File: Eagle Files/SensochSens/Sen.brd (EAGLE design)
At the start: 115.5 x 54.3 mm, 15 parts, among them U2 MIC5219, X1 ADC0-7

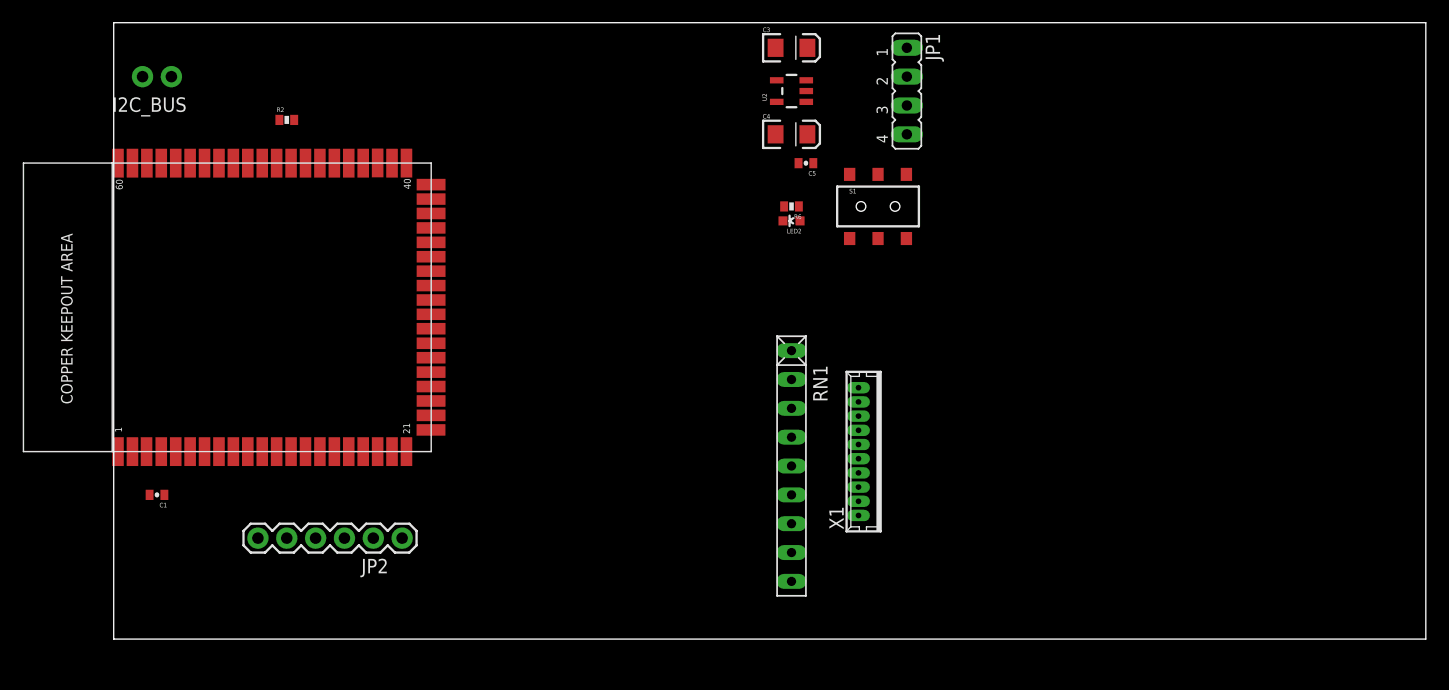
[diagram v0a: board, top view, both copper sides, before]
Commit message: 
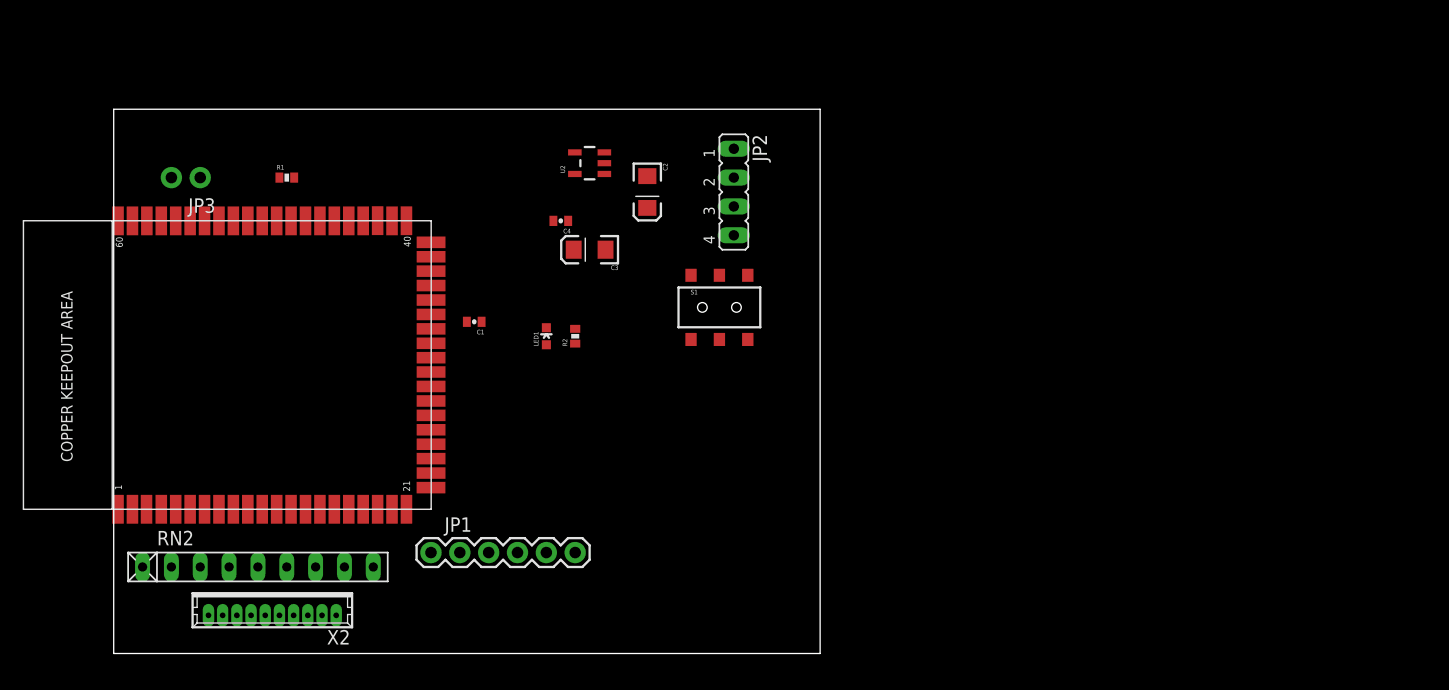
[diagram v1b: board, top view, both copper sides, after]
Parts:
- removed C5: 1uF, SparkFun-Passives:0402-CAP
- removed I2C_BUS: I2C_BUS, SparkFun-Connectors:1X02_NO_SILK
- removed LED2: RED, SparkFun-LED:LED-0603
- removed R6: 1k, SparkFun-Passives:0402-RES
- removed RN1: (no value), resistor-net:RN-9
- removed SMD1: SM700PC1SMD, Synapse_SM700PC1:SYNAPSE_SN700PC1
- removed X1: ADC0-7, con-molex:53047-10
- added C2: 10uF, SparkFun-Passives:EIA3216
- added JP3: I2C_BUS, SparkFun-Connectors:1X02_NO_SILK
- added LED1: RED, SparkFun-LED:LED-0603
- added R1: 100k, SparkFun-Passives:0402-RES
- added RN2: (no value), resistor-net:RN-9
- added U1: SM700PC1SMD, Synapse_SM700PC1:SYNAPSE_SN700PC1
- added X2: ADC0-7, con-molex:53047-10
- C4: value 10uF -> 1uF; device SparkFun-Passives:EIA3216 -> SparkFun-Passives:0402-CAP
- JP1: value LIPO_charger -> FTDI_BASICPTH; device jumper:JP4 -> SparkFun-Connectors:FTDI_BASIC
- JP2: value FTDI_BASICPTH -> LIPO_charger; device SparkFun-Connectors:FTDI_BASIC -> jumper:JP4
- R2: value 100k -> 1k
- moved JP1 58.4 mm to (27.9, 8.89), turned to 0 degrees
- moved JP2 42.2 mm to (54.6, 40.6), turned to 270 degrees
- moved C1 31.8 mm to (31.8, 29.2)
- moved R2 31.8 mm to (40.6, 27.9), turned to 90 degrees
- moved C3 25.1 mm to (41.9, 35.6), turned to 180 degrees
- moved C4 21.7 mm to (39.4, 38.1), turned to 180 degrees
- moved U2 18.9 mm to (41.9, 43.2)
- moved S1 16.6 mm to (53.3, 30.5)
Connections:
- removed net N$7: LED2.A, R6.1
- new net N$2: LED1.A, R2.1
- net 3.3V: now also C3.A, C4.1, JP1.VCC, R1.2, U1.P$12, U1.P$31, X2.1, X2.2; no longer C4.A, C5.1, JP2.VCC, R6.2, SMD1.P$12, SMD1.P$31, X1.1, X1.2
- net ADC0: now also RN2.2, U1.P$8, X2.3; no longer RN1.2, SMD1.P$8, X1.3
- net ADC1: now also RN2.3, U1.P$9, X2.4; no longer RN1.3, SMD1.P$9, X1.4
- net ADC2: now also RN2.4, U1.P$10, X2.5; no longer RN1.4, SMD1.P$10, X1.5
- net ADC3: now also RN2.5, U1.P$11, X2.6; no longer RN1.5, SMD1.P$11, X1.6
- net ADC4: now also RN2.6, U1.P$13, X2.7; no longer RN1.6, SMD1.P$13, X1.7
- net ADC5: now also RN2.7, U1.P$14, X2.8; no longer RN1.7, SMD1.P$14, X1.8
- net ADC6: now also RN2.8, U1.P$15, X2.9; no longer RN1.8, SMD1.P$15, X1.9
- net ADC7: now also RN2.9, U1.P$16, X2.10; no longer RN1.9, SMD1.P$16, X1.10
- net CTS2: now also JP1.CTS, U1.P$23; no longer JP2.CTS, SMD1.P$23
- net EN: now also JP2.4; no longer JP1.4
- net GND: now also C2.C, C4.2, JP1.GND, JP2.3, LED1.C, RN2.1, U1.P$1, U1.P$2, U1.P$22, U1.P$3, U1.P$38, U1.P$51, U1.P$58, U1.P$59, U1.P$60; no longer C4.C, C5.2, JP1.3, JP2.GND, LED2.C, RN1.1, SMD1.P$1, SMD1.P$2, SMD1.P$22, SMD1.P$3, SMD1.P$38, SMD1.P$51, SMD1.P$58, SMD1.P$59, SMD1.P$60
- net N$10: now also U1.P$17; no longer SMD1.P$17
- net N$11: now also U1.P$18; no longer SMD1.P$18
- net N$12: now also U1.P$19; no longer SMD1.P$19
- net PS: now also JP2.1; no longer JP1.1
- net RESET: now also R1.1, U1.P$49; no longer R2.1, SMD1.P$49
- net RTS2: now also JP1.DTR, U1.P$21; no longer JP2.DTR, SMD1.P$21
- net RX2: now also JP1.TXO, U1.P$24; no longer JP2.TXO, SMD1.P$24
- net SCL: now also JP3.2, U1.P$29; no longer I2C_BUS.2, SMD1.P$29
- net SDA: now also JP3.1, U1.P$28; no longer I2C_BUS.1, SMD1.P$28
- net TX2: now also JP1.RXI, U1.P$25; no longer JP2.RXI, SMD1.P$25
- net VBATT: now also JP2.2; no longer JP1.2
- net VIN: now also C2.A; no longer C3.A
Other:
- board size 115.5 x 54.3 mm -> 62.2 x 47.9 mm

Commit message: 
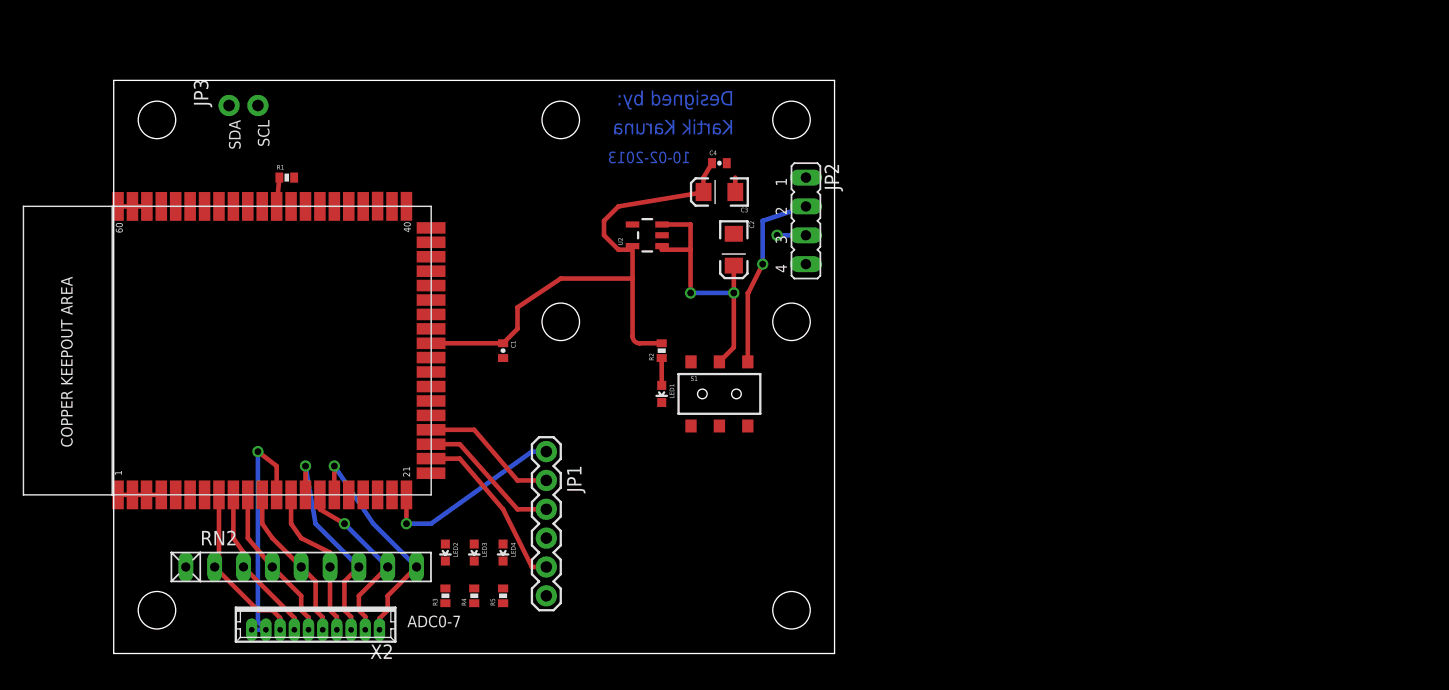
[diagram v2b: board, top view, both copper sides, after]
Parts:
- added JP10, JP4, JP5, JP6, JP7, JP8, JP9: STAND-OFF, SparkFun:STAND-OFF
- added LED2: GREEN, SparkFun-LED:LED-0603
- added LED3: YELLOW, SparkFun-LED:LED-0603
- added LED4: BLUE, SparkFun-LED:LED-0603
- added R3, R4, R5: 330, SparkFun-Passives:0402-RES
- RN2: value (none) -> 22K
- moved C4 14.9 mm to (53.3, 43.2), turned to 0 degrees
- moved JP1 13.5 mm to (38.1, 17.8), turned to 270 degrees
- moved C3 12.5 mm to (53.3, 40.6)
- moved LED1 11.4 mm to (48.3, 22.9), turned to 180 degrees
- moved C2 9.16 mm to (54.6, 35.6)
- moved U2 8.13 mm to (47.0, 36.8)
- moved R2 7.73 mm to (48.3, 26.7)
- moved S1 7.62 mm to (53.3, 22.9)
- moved JP2 6.84 mm to (61.0, 38.1)
- moved JP3 6.84 mm to (10.2, 48.3), turned to 0 degrees
- moved X2 4.02 mm to (17.8, 2.54)
- moved RN2 3.81 mm to (16.5, 7.62)
- moved C1 3.59 mm to (34.3, 26.7), turned to 270 degrees
- moved U1 1.27 mm to (29.2, 14.0)
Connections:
- removed net N$10: U1.P$17
- removed net N$11: U1.P$18
- removed net N$12: U1.P$19
- new net LED2: LED2.A, U1.P$17
- new net LED3: LED3.A, U1.P$18
- new net LED4: LED4.A, U1.P$19
- new net N$1: LED3.C, R4.2
- new net N$4: LED2.C, R3.2
- new net N$6: LED4.C, R5.2
- net GND: now also R3.1, R4.1, R5.1
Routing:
- net 3.3V: track 0.00 -> 70.3 mm, vias 0 -> 1
- net VIN: track 0.00 -> 24.2 mm, vias 0 -> 2
- net ADC7: track 0.00 -> 20.9 mm, vias 0 -> 1
- net ADC5: track 0.00 -> 19.4 mm, vias 0 -> 1
- net RTS2: track 0.00 -> 16.9 mm, vias 0 -> 1
- net VBATT: track 0.00 -> 16.8 mm, vias 0 -> 1
- net ADC6: track 0.00 -> 16.0 mm, vias 0 -> 1
- net ADC0: track 0.00 -> 15.4 mm
- net CTS2: track 0.00 -> 15.3 mm
- net ADC1: track 0.00 -> 14.0 mm
- net ADC3: track 0.00 -> 14.0 mm
- net ADC2: track 0.00 -> 14.0 mm
- net ADC4: track 0.00 -> 14.0 mm
- net RX2: track 0.00 -> 12.7 mm
- net TX2: track 0.00 -> 12.2 mm
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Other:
- board size 62.2 x 47.9 mm -> 63.5 x 50.5 mm
- board text added: "10-02-2013"
- board text added: "Designed by:"
- board text added: "Kartik Karuna"
- board text added: "SCL"
- board text added: "SDA"

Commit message: 
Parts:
- added U$1: KCSA03-102SMD_7SEG, cy-7-seg:SMD-7SEG
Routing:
- net 3.3V: track 70.3 -> 6.34 mm, vias 1 -> 0
- net VIN: track 24.2 -> 0.00 mm, vias 2 -> 0
- net ADC7: track 20.9 -> 0.00 mm, vias 1 -> 0
- net ADC5: track 19.4 -> 0.00 mm, vias 1 -> 0
- net RTS2: track 16.9 -> 0.00 mm, vias 1 -> 0
- net VBATT: track 16.8 -> 0.00 mm, vias 1 -> 0
- net ADC6: track 16.0 -> 0.00 mm, vias 1 -> 0
- net ADC0: track 15.4 -> 0.00 mm
- net CTS2: track 15.3 -> 0.00 mm
- net ADC1: track 14.0 -> 0.00 mm
- net ADC3: track 14.0 -> 0.00 mm
- net ADC2: track 14.0 -> 0.00 mm
- net ADC4: track 14.0 -> 0.00 mm
- net RX2: track 12.7 -> 0.00 mm
- net TX2: track 12.2 -> 0.00 mm
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
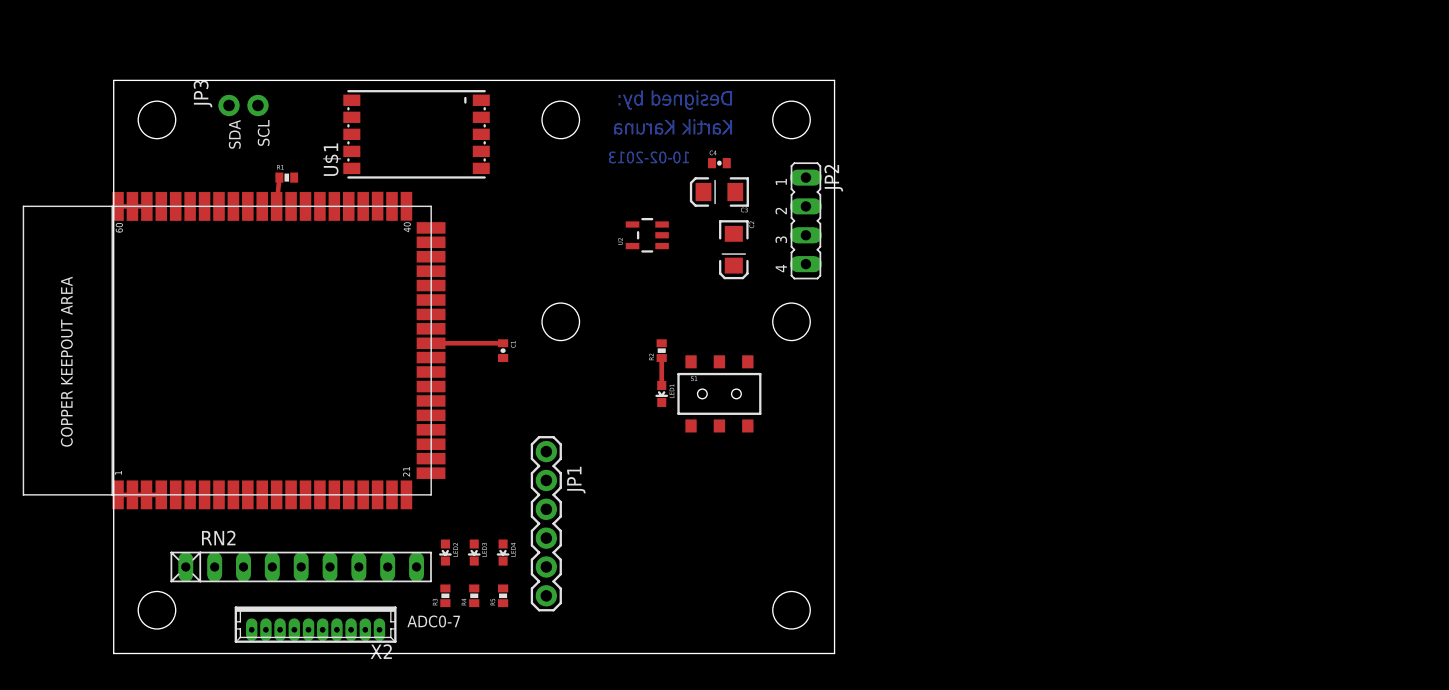
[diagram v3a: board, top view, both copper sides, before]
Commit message: 
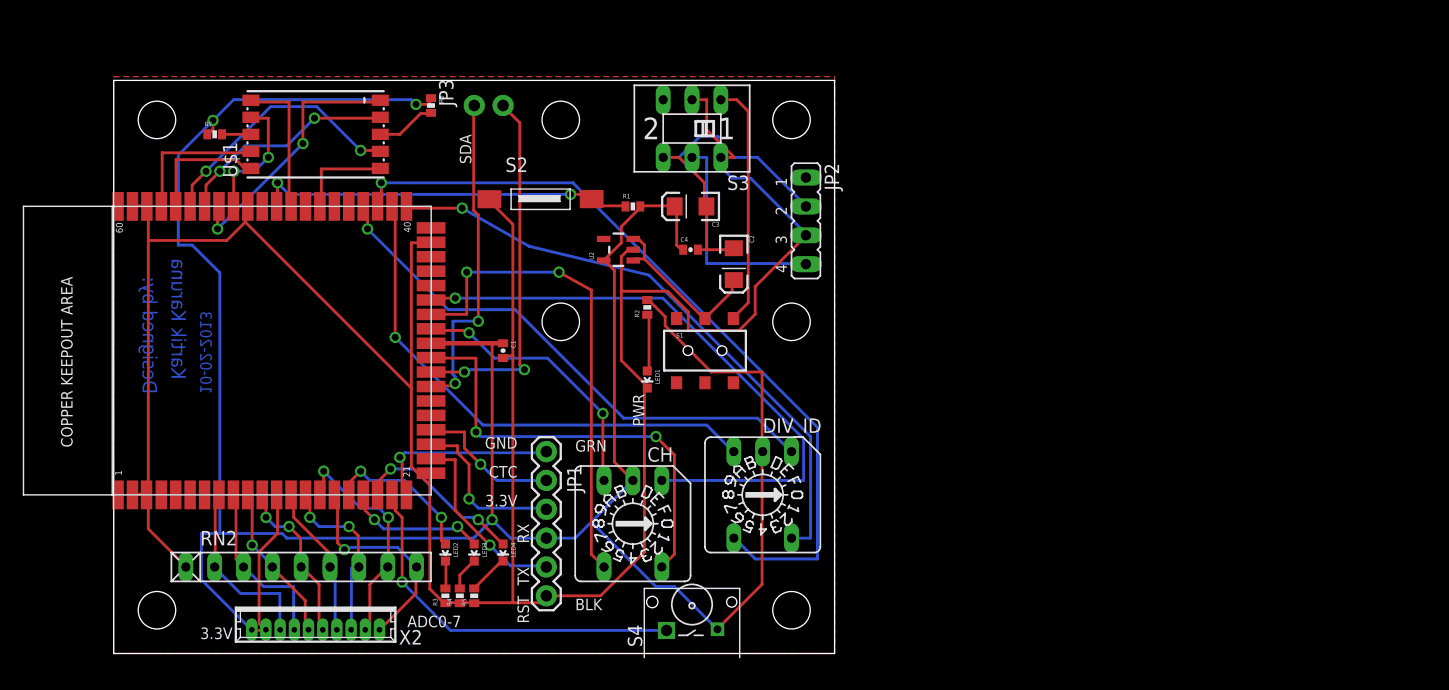
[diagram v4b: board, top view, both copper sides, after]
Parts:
- added CH, DIV_ID: (no value), switch-dil:A1353HEX
- added R6, R7: 330, SparkFun-Passives:0402-RES
- added S2: RESET, cy_fsmsm:TYCO_FSM
- added S3: (no value), switch:A68-A31
- added S4: TOGGLE, cy_fsmsm:TYCO_FSMRACDA
- JP1: value FTDI_BASICPTH -> FTDI
- moved R1 30.6 mm to (45.7, 39.4)
- moved JP3 21.6 mm to (31.8, 48.3)
- moved U$1 8.89 mm to (17.8, 45.7)
- moved C4 8.03 mm to (50.8, 35.6)
- moved S1 4.02 mm to (52.1, 26.7)
- moved R2 4.02 mm to (47.0, 30.5)
- moved C3 2.84 mm to (50.8, 39.4)
- moved U2 2.84 mm to (44.5, 35.6)
- moved R5 2.54 mm to (31.8, 5.08)
- moved LED1 1.80 mm to (47.0, 24.1)
- moved C2 1.27 mm to (54.6, 34.3)
- moved R4 1.27 mm to (30.5, 5.08)
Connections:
- new net 7SEG_A: U$1.7, U1.P$57
- new net 7SEG_B: U$1.6, U1.P$56
- new net 7SEG_C: U$1.4, U1.P$55
- new net 7SEG_D: U$1.2, U1.P$54
- new net 7SEG_DP: U$1.5, U1.P$46
- new net 7SEG_E: U$1.1, U1.P$53
- new net 7SEG_F: U$1.9, U1.P$52
- new net 7SEG_G: U$1.10, U1.P$48
- new net CH_1: CH.1, U1.P$34
- new net CH_2: CH.2, U1.P$33
- new net CH_3: CH.4, U1.P$32
- new net CH_4: CH.8, U1.P$30
- new net DIV_1: DIV_ID.1, U1.P$43
- new net DIV_2: DIV_ID.2, U1.P$42
- new net DIV_3: DIV_ID.4, U1.P$41
- new net DIV_4: DIV_ID.8, U1.P$40
- new net N$3: R6.2, U$1.3
- new net N$5: R7.2, U$1.8
- new net TOGL: S4.1, U1.P$20
- new net VCC1: S1.3, S3.1
- net 3.3V: now also CH.C, DIV_ID.C, R6.1, R7.1, S4.2
- net EN: now also S3.5
- net GND: now also S2.1, S3.6
- net RESET: now also S2.2
- net VBATT: now also S3.2, S3.4; no longer S1.3
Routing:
- net GND: track 6.10 -> 244.5 mm
- net 3.3V: track 6.34 -> 236.2 mm, vias 0 -> 3
- net DIV_2: track 0.00 -> 69.3 mm, vias 0 -> 1
- net CH_1: track 0.00 -> 54.2 mm, vias 0 -> 1
- net DIV_4: track 0.00 -> 53.4 mm, vias 0 -> 1
- net DIV_1: track 0.00 -> 47.6 mm, vias 0 -> 1
- net DIV_3: track 0.00 -> 45.6 mm, vias 0 -> 1
- net CH_2: track 0.00 -> 43.1 mm, vias 0 -> 2
- net CH_4: track 0.00 -> 39.1 mm, vias 0 -> 2
- net TOGL: track 0.00 -> 33.1 mm, vias 0 -> 1
- net SCL: track 0.00 -> 32.3 mm, vias 0 -> 2
- net RESET: track 2.55 -> 34.1 mm, vias 0 -> 2
- net SDA: track 0.00 -> 29.3 mm, vias 0 -> 2
- net CH_3: track 0.00 -> 24.3 mm, vias 0 -> 2
- net 7SEG_E: track 0.00 -> 23.2 mm, vias 0 -> 2
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- added copper zone on layer 1, net GND
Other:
- board text added: "3.3V"
- board text added: "A"
- board text added: "B"
- board text added: "BLK"
- board text added: "C"
- board text added: "CTC"
- board text added: "GND"
- board text added: "GRN"
- board text added: "PWR"
- board text added: "RST"
- board text added: "RX"
- board text added: "TX"
